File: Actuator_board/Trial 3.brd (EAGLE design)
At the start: 76.2 x 50.8 mm, 42 parts, among them CON1 SM03B-GHS-TB, CON2 SM03B-GHS-TB, CON3 MOLEX_5566-2, Q3 IRL6372TRPBF, Q4 IRL6372TRPBF, U3 TCAN1042HVDR, U4 PCA9685PW, U5 TEENSY_3.1_BASIC_2, X1 OSTVN05A150, X2 MOLEX_5566-4

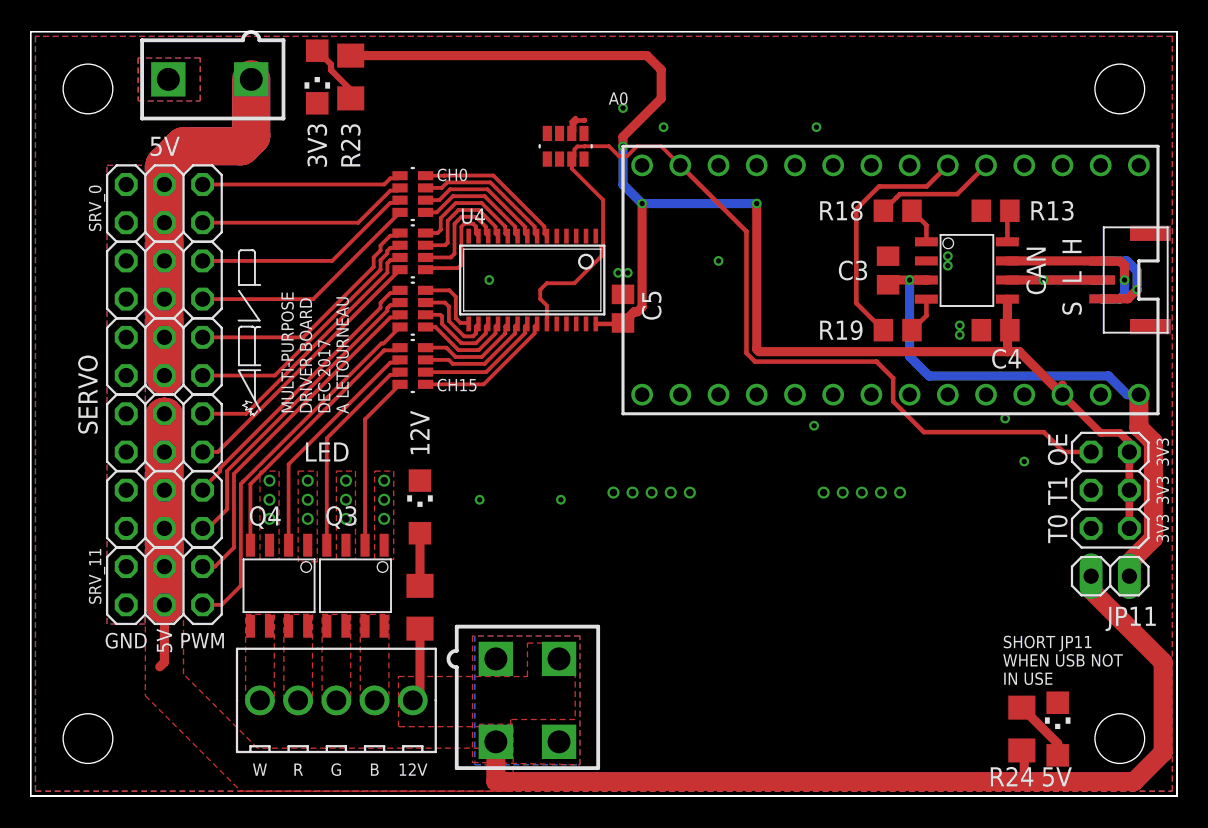
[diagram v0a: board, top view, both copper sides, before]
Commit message: Realigned Parts
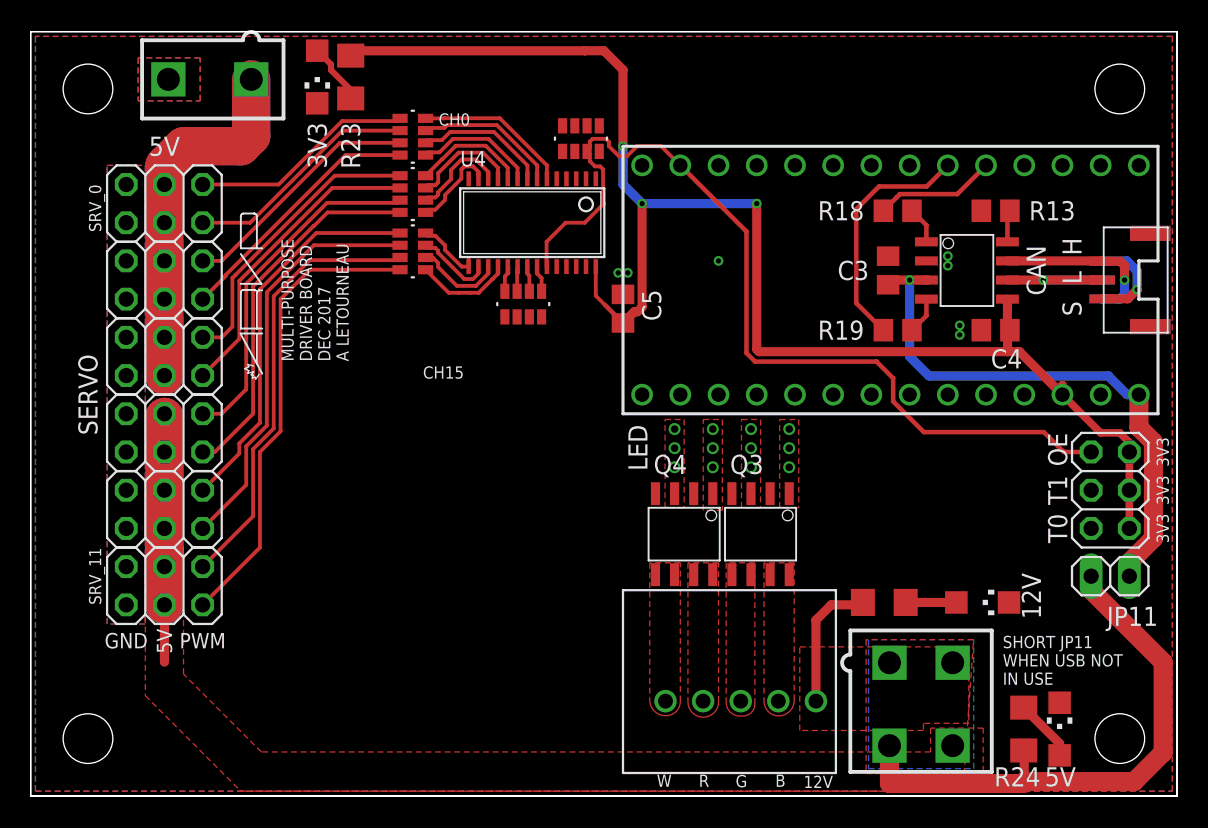
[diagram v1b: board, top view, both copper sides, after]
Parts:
- removed X1: OSTVN05A150, dropper_torpedo_v3:OSTVN05A150
- added U$1: SCREWLESS_TERMINAL_HEADERSCREWLESS_TERMINAL_HEADER, Screwless-terminal-header:1989777_TERMINALHEADER
- moved LED5 37.9 mm to (63.3, 12.9), turned to 270 degrees
- moved R25 30.9 mm to (56.7, 12.9), turned to 180 degrees
- moved Q3 27.1 mm to (48.5, 17.4)
- moved Q4 27.1 mm to (43.4, 17.4)
- moved X2 26.2 mm to (59.2, 6.10)
- moved R17 8.42 mm to (32.7, 32.7), turned to 90 degrees
- moved R15 3.81 mm to (25.4, 40.0)
- moved R16 3.81 mm to (25.4, 36.2)
- moved U4 3.81 mm to (33.3, 38.1)
- moved R14 3.81 mm to (25.4, 43.8)
- moved U$5 2.44 mm to (15.4, 27.8)
- moved R26 1.14 mm to (36.6, 43.7)
- moved R24 0.13 mm to (66.0, 4.45)
- moved LED4 0.13 mm to (68.4, 4.45)
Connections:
- net +12V: now also U$1.P$5; no longer X1.P$5
- net LED_DRAIN0: now also U$1.P$4; no longer X1.P$4
- net LED_DRAIN1: now also U$1.P$3; no longer X1.P$3
- net LED_DRAIN2: now also U$1.P$2; no longer X1.P$2
- net LED_DRAIN3: now also U$1.P$1; no longer X1.P$1
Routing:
- net +5V: track 109.6 -> 73.6 mm
- net LED_GATE3: track 17.8 -> 0.18 mm
- net LED_GATE2: track 15.7 -> 0.00 mm
- net LED_GATE1: track 13.8 -> 0.00 mm
- net LED_GATE0: track 11.7 -> 0.00 mm
- net PWM_CH15: track 9.35 -> 1.76 mm
- net PWM_SERVO8: track 19.0 -> 25.8 mm
- net PWM_SERVO9: track 20.9 -> 27.6 mm
- net PWM_CH14: track 8.36 -> 1.70 mm
- net PWM_SERVO7: track 18.1 -> 24.7 mm
- net PWM_SERVO11: track 24.7 -> 31.2 mm
- net PWM_SERVO10: track 22.9 -> 29.4 mm
- net PWM_CH13: track 7.59 -> 1.89 mm
- net PWM_SERVO6: track 17.8 -> 23.1 mm
- net PWM_CH12: track 6.90 -> 1.75 mm
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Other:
- board text removed: "A0"
